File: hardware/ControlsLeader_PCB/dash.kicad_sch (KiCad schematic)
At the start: 47 parts, among them Q1 NMOS, Q10 NMOS, Q11 NMOS, Q12 NMOS, Q13 NMOS, Q14 NMOS, Q3 NMOS, Q4 NMOS, Q7 NMOS, Q8 NMOS

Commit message: Board review
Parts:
- removed C10, C12, C14: 5uF, Capacitor_SMD:C_0805_2012Metric, symbol Device:C_Small

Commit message: Schematic Backup
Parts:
- removed C11, C13, C3, C4, C5, C6, C7, C8, C9: 5uF, Capacitor_SMD:C_0805_2012Metric, symbol Device:C_Small
- removed Q1, Q10, Q11, Q12, Q13, Q14, Q3, Q4, Q7, Q8: NMOS, symbol Simulation_SPICE:NMOS
- removed R1, R2, R20, R22, R23, R24, R26, R27, R28, R3, R4, R5, R6, R7: 100k, symbol Device:R
- removed R12, R13, R14, R15, R25: 10k, Resistor_SMD:R_0805_2012Metric, symbol Device:R
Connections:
- net NMOS Switch8/24V_Signal: now reaches Regen_Enable1.2
- net NMOS Switch4/24V_Signal: now reaches Ignition1.2
- net NMOS Switch7/24V_Signal: now reaches Cruise_Set1.2
- net NMOS Switch2/24V_Signal: now reaches Gear1.4
- net NMOS Switch9/24V_Signal: now reaches Hazard1.2
- net NMOS Switch5/24V_Signal: now reaches Ignition1.4
- net NMOS Switch/24V_Signal: now reaches Gear1.1
- net NMOS Switch6/24V_Signal: now reaches Cruise_Enable1.2
- net NMOS Switch3/24V_Signal: now reaches Ignition1.1
- net NMOS Switch1/24V_Signal: now reaches Gear1.2
- net +24V renamed 24V_PWR
- net 24V_PWR: no longer Cruise_Enable1.1
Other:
- added sheet NMOS Switch (NMOS_SW.kicad_sch)
- added sheet NMOS Switch1 (NMOS_SW.kicad_sch)
- added sheet NMOS Switch2 (NMOS_SW.kicad_sch)
- added sheet NMOS Switch3 (NMOS_SW.kicad_sch)
- added sheet NMOS Switch4 (NMOS_SW.kicad_sch)
- added sheet NMOS Switch5 (NMOS_SW.kicad_sch)
- added sheet NMOS Switch6 (NMOS_SW.kicad_sch)
- added sheet NMOS Switch7 (NMOS_SW.kicad_sch)
- added sheet NMOS Switch8 (NMOS_SW.kicad_sch)
- added sheet NMOS Switch9 (NMOS_SW.kicad_sch)
- moved on the sheet: Cruise_Enable1, Cruise_Set1, Gear1, Hazard1, Ignition1, Regen_Enable1

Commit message: DONE!!! - just need to add footprints + part #s)
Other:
- note added: "Cruise, Regen, and Hazard Switches"
- note added: "Ignition & Gear Switches"
- moved on the sheet: Cruise_Enable1, Cruise_Set1, Hazard1, Regen_Enable1

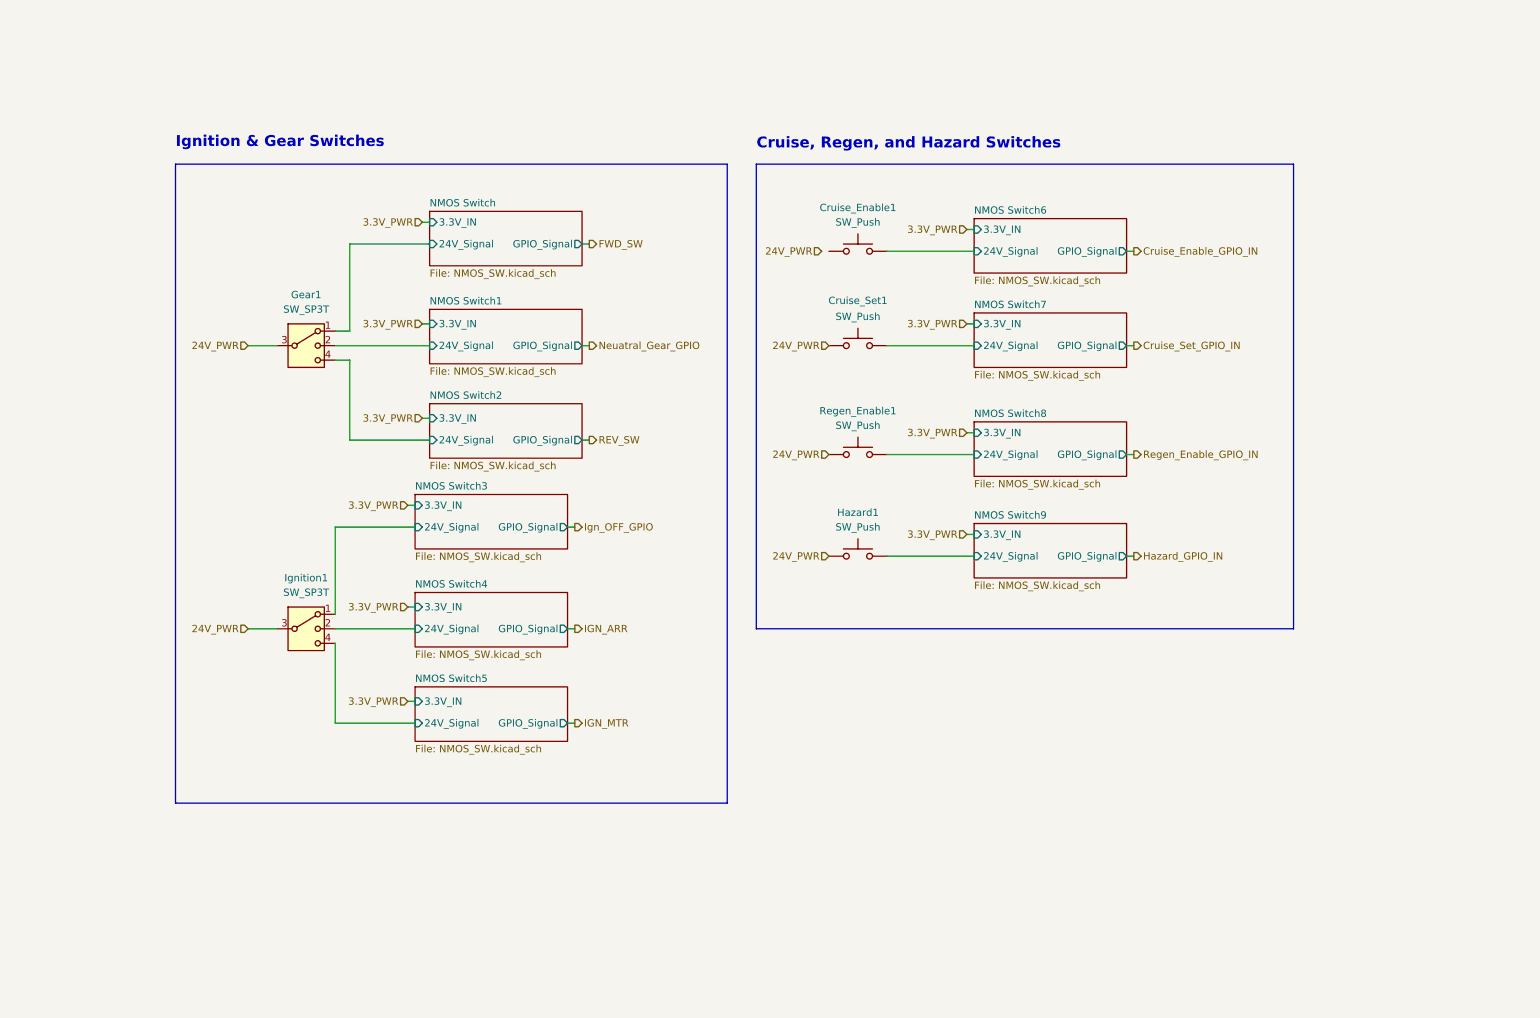
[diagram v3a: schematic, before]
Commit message: Schematic Ready for Review - Just need FET footprints to be confirmed
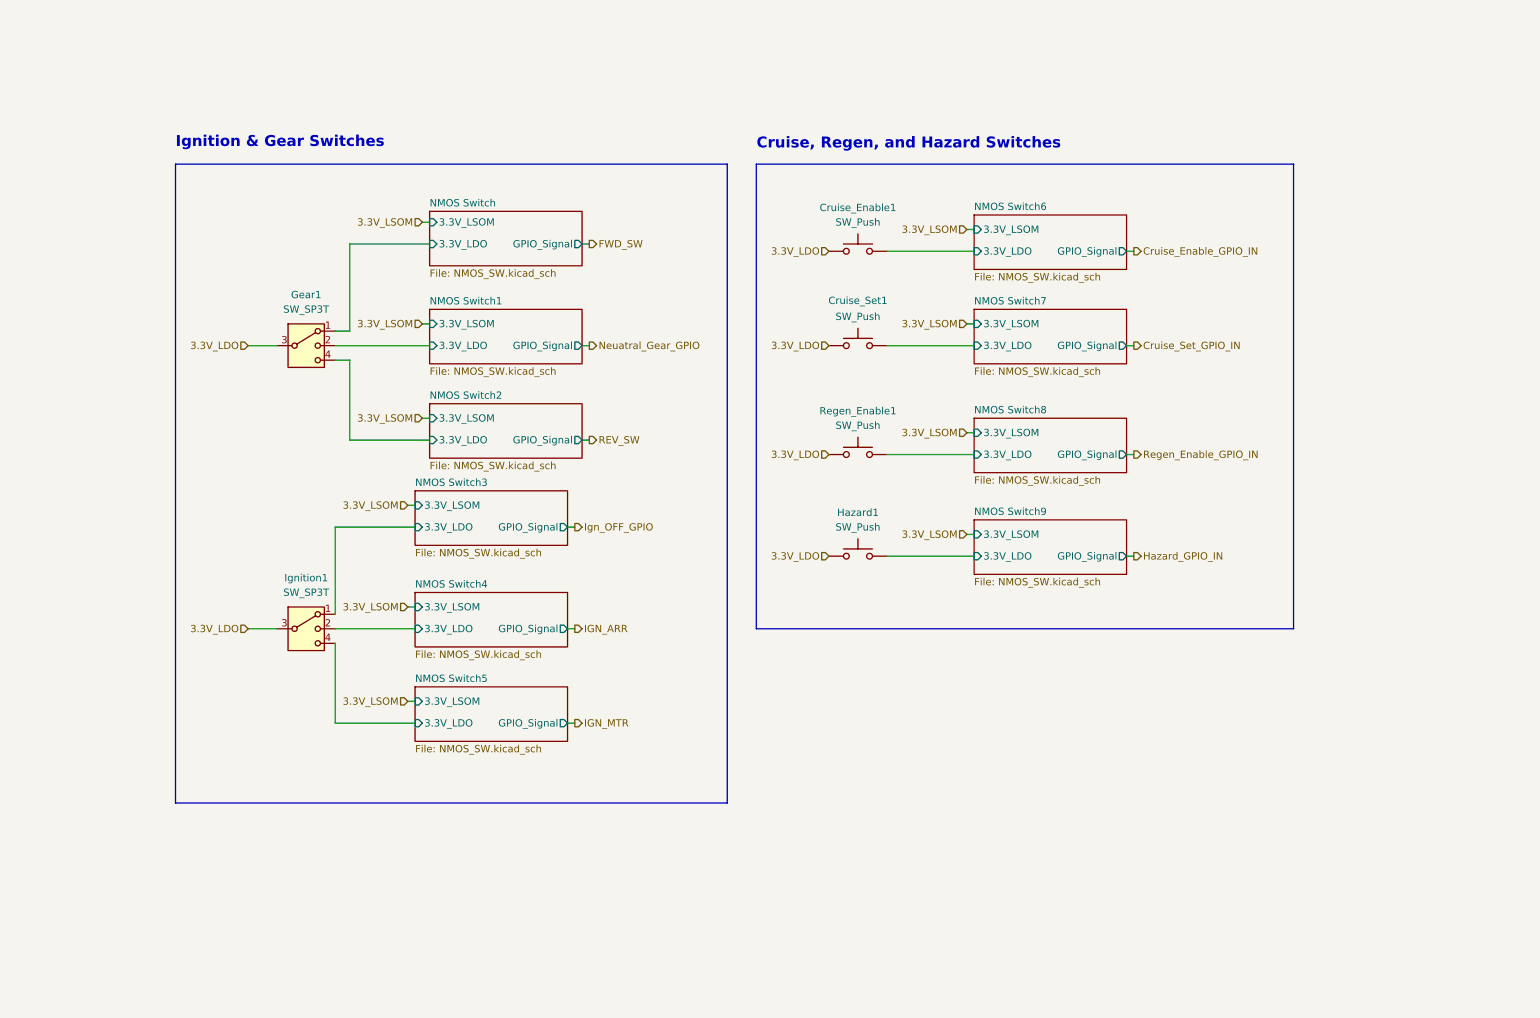
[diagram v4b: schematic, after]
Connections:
- net 24V_PWR is gone; now on net 3.3V_LDO: Cruise_Set1.1, Gear1.3, Hazard1.1, Ignition1.3, Regen_Enable1.1
- net 3.3V_LDO: now reaches Cruise_Enable1.1
- net NMOS Switch/24V_Signal renamed NMOS Switch/3.3V_LDO
- net NMOS Switch1/24V_Signal renamed NMOS Switch1/3.3V_LDO
- net NMOS Switch2/24V_Signal renamed NMOS Switch2/3.3V_LDO
- net NMOS Switch3/24V_Signal renamed NMOS Switch3/3.3V_LDO
- net NMOS Switch4/24V_Signal renamed NMOS Switch4/3.3V_LDO
- net NMOS Switch5/24V_Signal renamed NMOS Switch5/3.3V_LDO
- net NMOS Switch6/24V_Signal renamed NMOS Switch6/3.3V_LDO
- net NMOS Switch7/24V_Signal renamed NMOS Switch7/3.3V_LDO
- net NMOS Switch8/24V_Signal renamed NMOS Switch8/3.3V_LDO
- net NMOS Switch9/24V_Signal renamed NMOS Switch9/3.3V_LDO
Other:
- sheet NMOS Switch ports: added 3.3V_LDO, 3.3V_LSOM; removed 24V_Signal, 3.3V_IN
- sheet NMOS Switch1 ports: added 3.3V_LDO, 3.3V_LSOM; removed 24V_Signal, 3.3V_IN
- sheet NMOS Switch2 ports: added 3.3V_LDO, 3.3V_LSOM; removed 24V_Signal, 3.3V_IN
- sheet NMOS Switch3 ports: added 3.3V_LDO, 3.3V_LSOM; removed 24V_Signal, 3.3V_IN
- sheet NMOS Switch4 ports: added 3.3V_LDO, 3.3V_LSOM; removed 24V_Signal, 3.3V_IN
- sheet NMOS Switch5 ports: added 3.3V_LDO, 3.3V_LSOM; removed 24V_Signal, 3.3V_IN
- sheet NMOS Switch6 ports: added 3.3V_LDO, 3.3V_LSOM; removed 24V_Signal, 3.3V_IN
- sheet NMOS Switch7 ports: added 3.3V_LDO, 3.3V_LSOM; removed 24V_Signal, 3.3V_IN
- sheet NMOS Switch8 ports: added 3.3V_LDO, 3.3V_LSOM; removed 24V_Signal, 3.3V_IN
- sheet NMOS Switch9 ports: added 3.3V_LDO, 3.3V_LSOM; removed 24V_Signal, 3.3V_IN

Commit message: Ready for final review
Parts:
- added J11: EStop1, Connector_Molex:Molex_Micro-Fit_3.0_43650-0215_1x02_P3.00mm_Vertical, symbol Connector_Generic:Conn_01x02
- added J12: EStop2, Connector_Molex:Molex_Micro-Fit_3.0_43650-0215_1x02_P3.00mm_Vertical, symbol Connector_Generic:Conn_01x02
- added J13, J9: Supp_In, Connector_Molex:Molex_Micro-Fit_3.0_43650-0215_1x02_P3.00mm_Vertical, symbol Connector_Generic:Conn_01x02
- added J14: EStop3, Connector_Molex:Molex_Micro-Fit_3.0_43650-0215_1x02_P3.00mm_Vertical, symbol Connector_Generic:Conn_01x02
- Cruise_Enable1, Cruise_Set1, Hazard1, Regen_Enable1: Distributor Link (none) -> https://www.amazon.com/Gebildet-Waterproof-Momentary-Lockle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; Manufacturer (none) -> Amazon
- Gear1, Ignition1: Distributor Link (none) -> https://www.digikey.com/en/products/detail/c-k/A12505RNZQ/2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; Manufacturer (none) -> DigiKey
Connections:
- new net Contactor_IN1: J11.2 (Pin_2), J14.2 (Pin_2)
- new net Contactor_OUT1: J11.1 (Pin_1), J12.2 (Pin_2)
- new net Contactor_OUT2: J12.1 (Pin_1), J14.1 (Pin_1)
- new net LV-: J13.2 (Pin_2), J9.2 (Pin_2)
- new net LV_EN: J13.1 (Pin_1), J9.1 (Pin_1)
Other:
- note added: "E-Stop Connectors (2.5A Max)"
- note added: "Supplemental Power Switch"
- moved on the sheet: Cruise_Enable1, Cruise_Set1, Gear1, Hazard1, Ignition1, Regen_Enable1

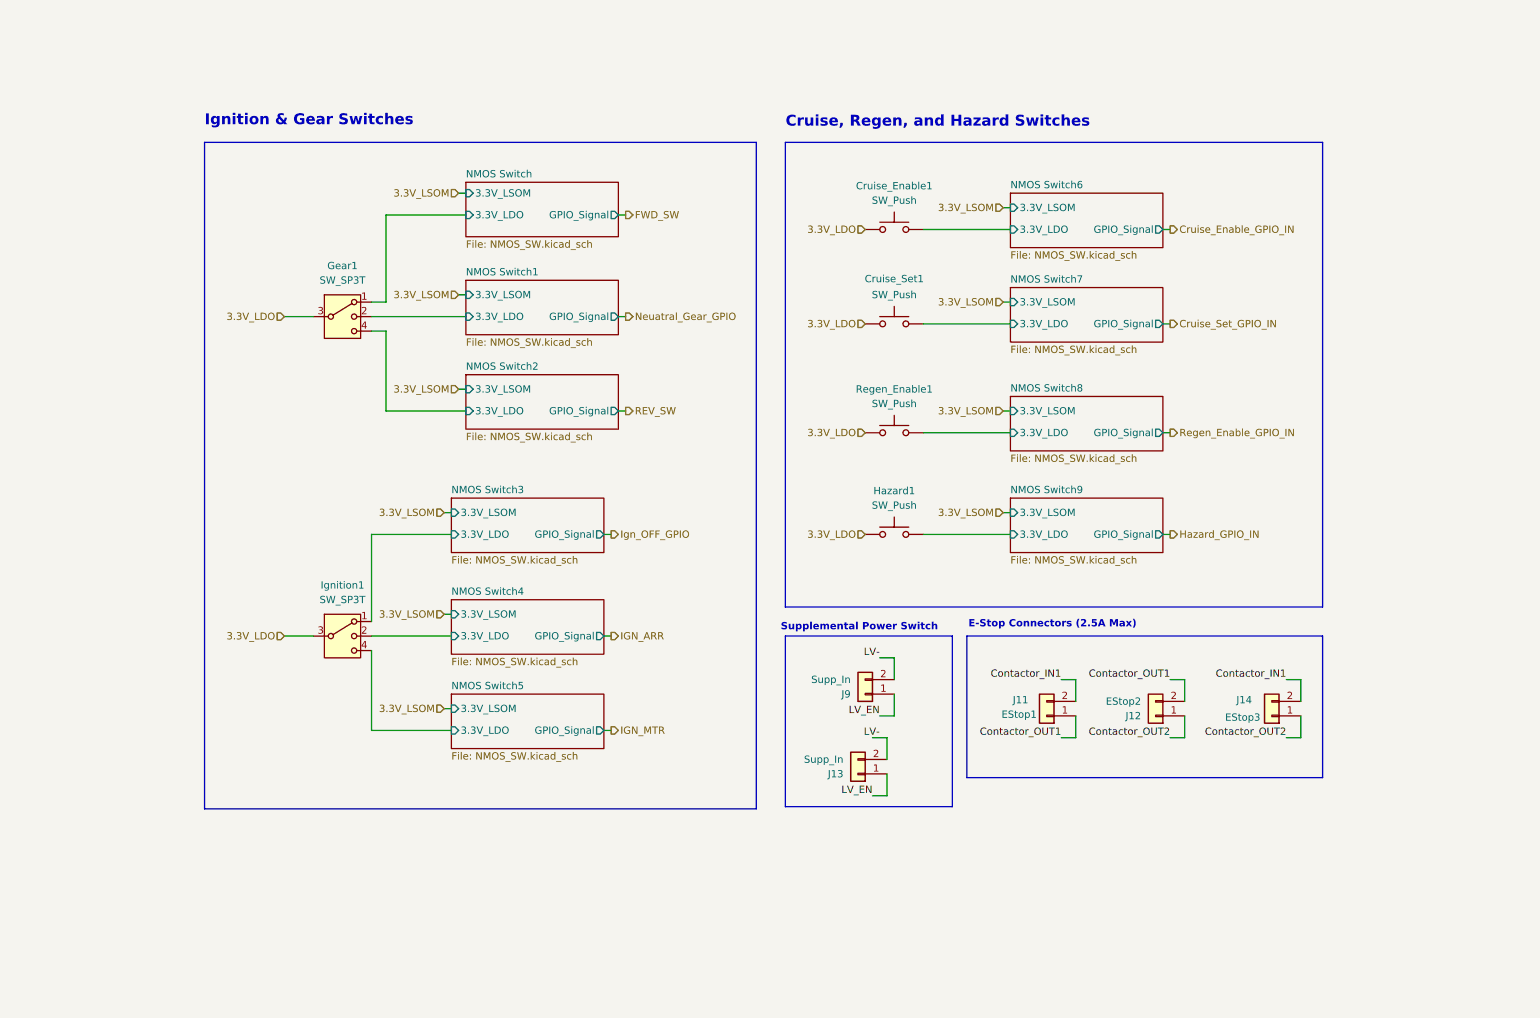
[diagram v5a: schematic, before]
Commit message: Updated LSOM status LED and horn 24v signal connector layout
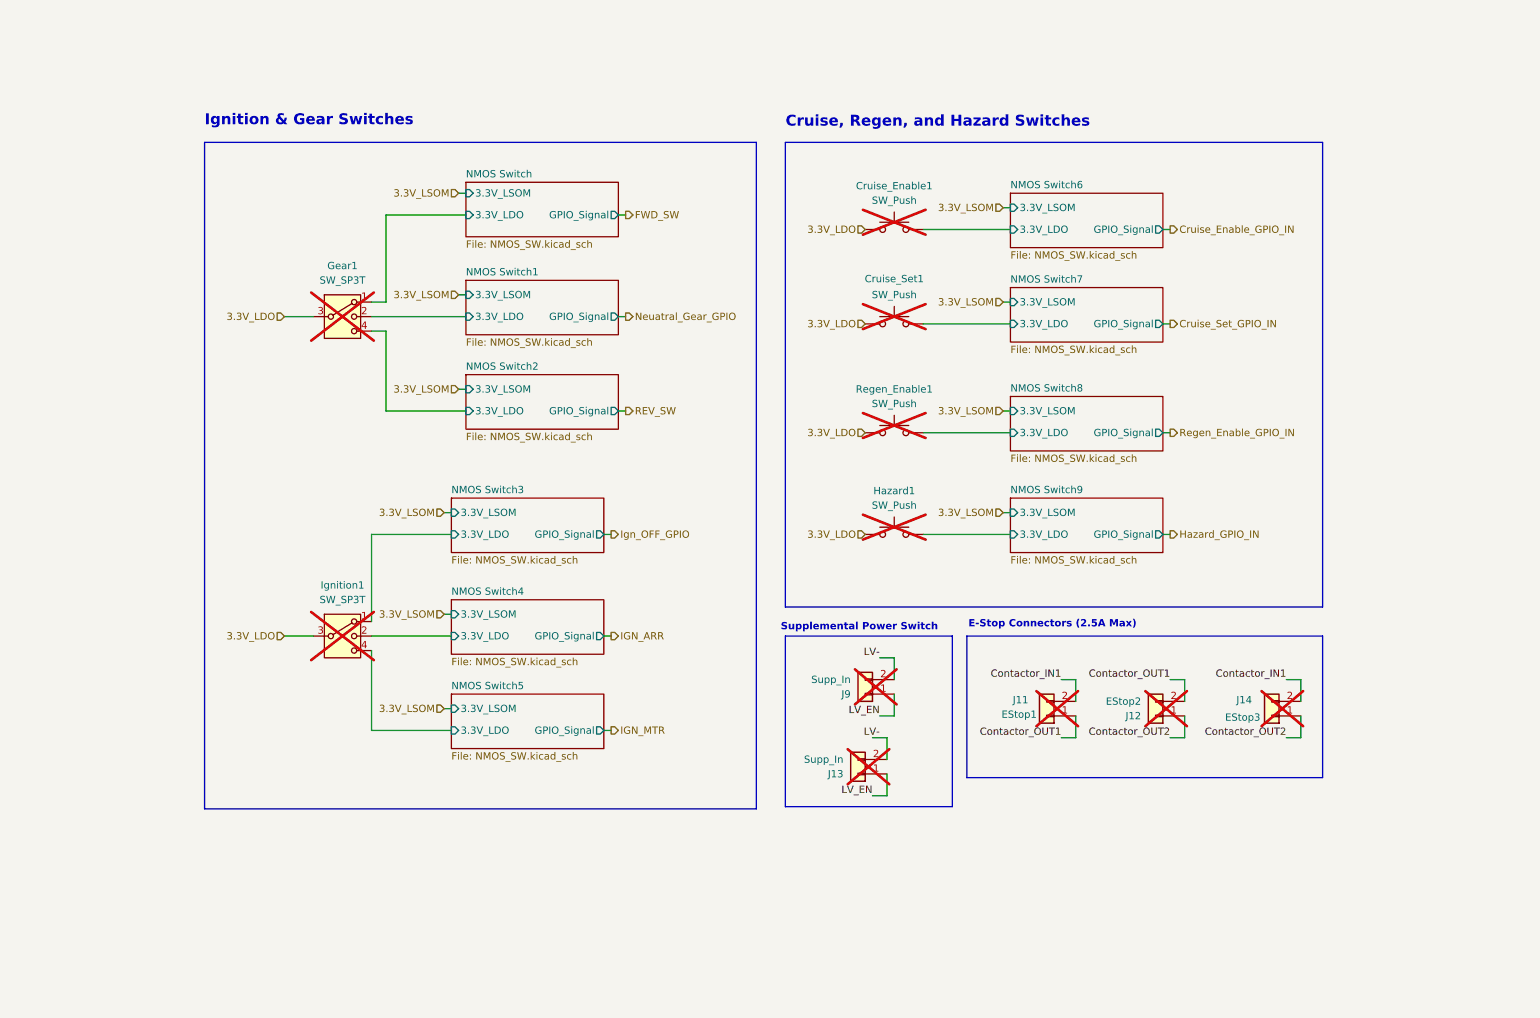
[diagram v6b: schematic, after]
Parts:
- Cruise_Enable1, Cruise_Set1, Gear1, Hazard1, Ignition1, J11, J12, J13, J14, J9, Regen_Enable1: now not fitted
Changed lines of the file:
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@@
 		(exclude_from_sim no)
 		(in_bom yes)
-		(on_board yes)
-		(dnp no)
+		(on_board no)
+		(dnp yes)
 		(property "Reference" "J12"
 			(at 214.63 139.7001 0)
@@
 		(exclude_from_sim no)
 		(in_bom yes)
-		(on_board yes)
-		(dnp no)
+		(on_board no)
+		(dnp yes)
 		(fields_autoplaced yes)
 		(property "Reference" "Cruise_Enable1"
@@
 		(exclude_from_sim no)
 		(in_bom yes)
-		(on_board yes)
-		(dnp no)
+		(on_board no)
+		(dnp yes)
 		(property "Reference" "J11"
 			(at 193.548 136.906 0)
@@
 		(exclude_from_sim no)
 		(in_bom yes)
-		(on_board yes)
-		(dnp no)
+		(on_board no)
+		(dnp yes)
 		(fields_autoplaced yes)
 		(property "Reference" "Ignition1"
@@
 		(exclude_from_sim no)
 		(in_bom yes)
-		(on_board yes)
-		(dnp no)
+		(on_board no)
+		(dnp yes)
 		(fields_autoplaced yes)
 		(property "Reference" "Regen_Enable1"
@@
 		(exclude_from_sim no)
 		(in_bom yes)
-		(on_board yes)
-		(dnp no)
+		(on_board no)
+		(dnp yes)
 		(fields_autoplaced yes)
 		(property "Reference" "J9"
@@
 		(exclude_from_sim no)
 		(in_bom yes)
-		(on_board yes)
-		(dnp no)
+		(on_board no)
+		(dnp yes)
 		(fields_autoplaced yes)
 		(property "Reference" "J13"
@@
 		(exclude_from_sim no)
 		(in_bom yes)
-		(on_board yes)
-		(dnp no)
+		(on_board no)
+		(dnp yes)
 		(property "Reference" "J14"
 			(at 232.664 136.906 0)
@@
 		(exclude_from_sim no)
 		(in_bom yes)
-		(on_board yes)
-		(dnp no)
+		(on_board no)
+		(dnp yes)
 		(fields_autoplaced yes)
 		(property "Reference" "Hazard1"
@@
 		(exclude_from_sim no)
 		(in_bom yes)
-		(on_board yes)
-		(dnp no)
+		(on_board no)
+		(dnp yes)
 		(property "Reference" "Cruise_Set1"
 			(at 171.45 63.246 0)
@@
 		(exclude_from_sim no)
 		(in_bom yes)
-		(on_board yes)
-		(dnp no)
+		(on_board no)
+		(dnp yes)
 		(fields_autoplaced yes)
 		(property "Reference" "Gear1"
